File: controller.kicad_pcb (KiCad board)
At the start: 2 copper layers, 59.7 x 49.5 mm, 11 parts, among them J1 Conn_01x03_Male, J2 Conn_01x03_Male, J3 Conn_01x03_Female, J4 Conn_01x03_Male, J5 Conn_01x02_Male

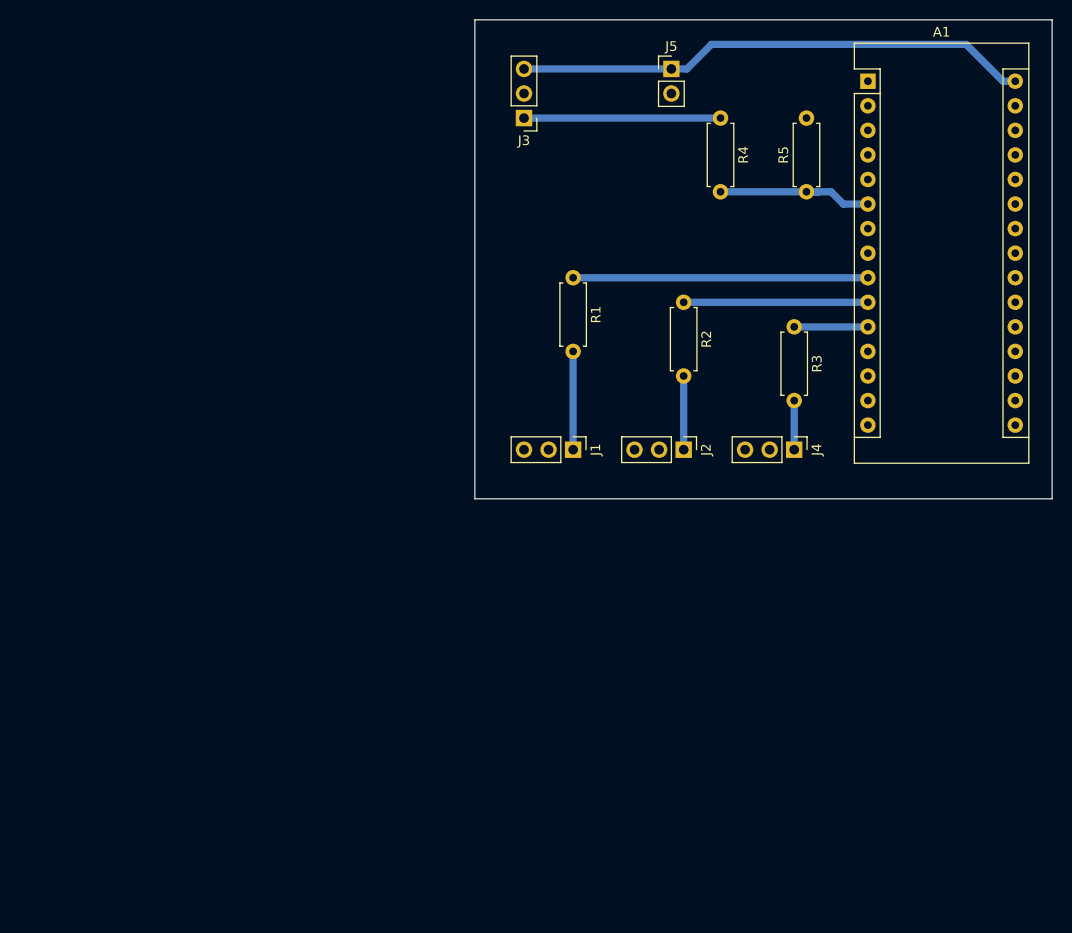
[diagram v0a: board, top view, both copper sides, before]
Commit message: Added max485 and power circuitry
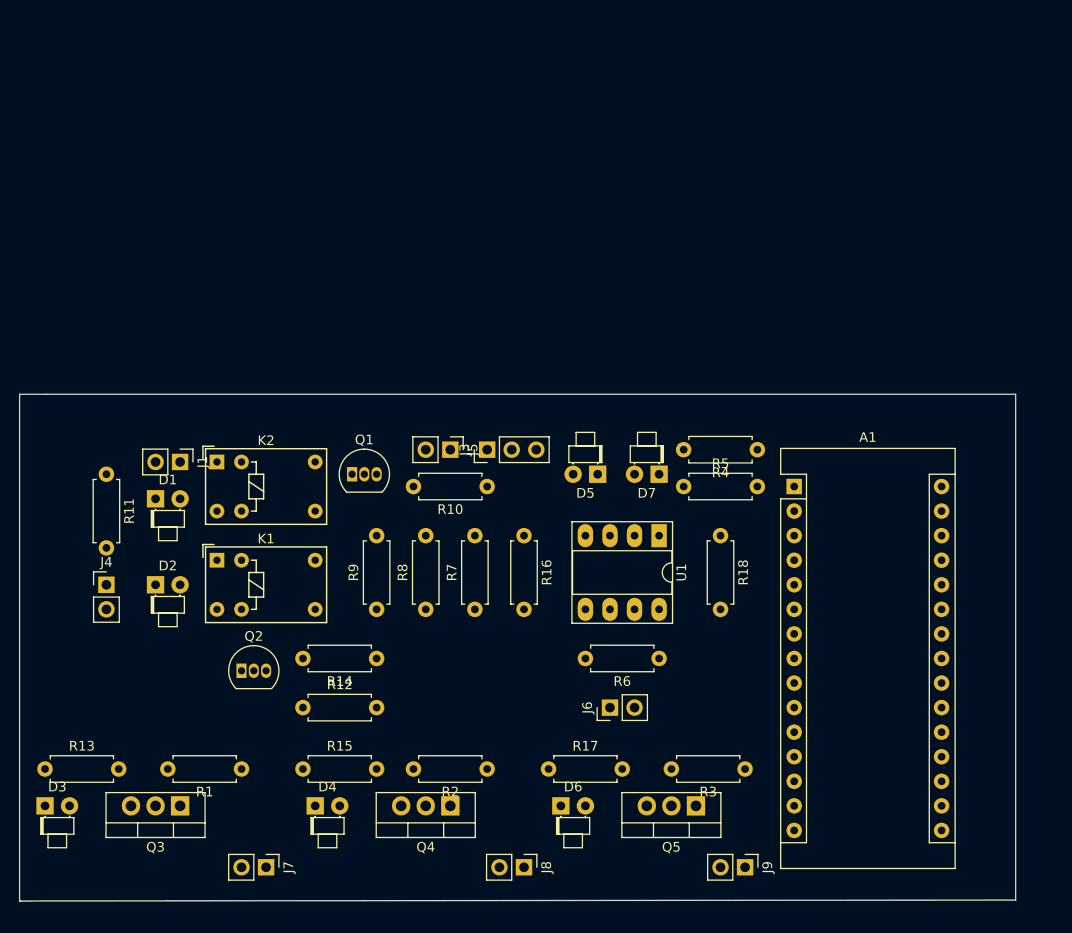
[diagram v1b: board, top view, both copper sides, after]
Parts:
- removed J2: Conn_01x03_Male, Connector_PinHeader_2.54mm:PinHeader_1x03_P2.54mm_Vertical
- added D1: LED, LED_THT:LED_D1.8mm_W1.8mm_H2.4mm_Horizontal_O1.27mm_Z1.6mm, F.Cu at (53.3, 94.0)
- added D2: LED, LED_THT:LED_D1.8mm_W1.8mm_H2.4mm_Horizontal_O1.27mm_Z1.6mm, F.Cu at (53.3, 102.9)
- added D3: LED, LED_THT:LED_D1.8mm_W1.8mm_H2.4mm_Horizontal_O1.27mm_Z1.6mm, F.Cu at (41.9, 125.7)
- added D4: LED, LED_THT:LED_D1.8mm_W1.8mm_H2.4mm_Horizontal_O1.27mm_Z1.6mm, F.Cu at (69.8, 125.7)
- added D5: LED, LED_THT:LED_D1.8mm_W1.8mm_H2.4mm_Horizontal_O1.27mm_Z1.6mm, F.Cu at (99.1, 91.4)
- added D6: LED, LED_THT:LED_D1.8mm_W1.8mm_H2.4mm_Horizontal_O1.27mm_Z1.6mm, F.Cu at (95.2, 125.7)
- added D7: LED, LED_THT:LED_D1.8mm_W1.8mm_H2.4mm_Horizontal_O1.27mm_Z1.6mm, F.Cu at (105.4, 91.4)
- added J6: Conn_01x02, Connector_PinHeader_2.54mm:PinHeader_1x02_P2.54mm_Vertical, F.Cu at (100.3, 115.6)
- added J7: Conn_01x02, Connector_PinHeader_2.54mm:PinHeader_1x02_P2.54mm_Vertical, F.Cu at (64.8, 132.1)
- added J8: Conn_01x02, Connector_PinHeader_2.54mm:PinHeader_1x02_P2.54mm_Vertical, F.Cu at (91.4, 132.1)
- added J9: Conn_01x02, Connector_PinHeader_2.54mm:PinHeader_1x02_P2.54mm_Vertical, F.Cu at (114.3, 132.1)
- added K1: Y14x-1C-xxDS, Relay_THT:Relay_SPDT_HsinDa_Y14, F.Cu at (59.7, 100.3)
- added K2: Y14x-1C-xxDS, Relay_THT:Relay_SPDT_HsinDa_Y14, F.Cu at (59.7, 90.2)
- added Q1: PN2222A, Package_TO_SOT_THT:TO-92_Inline, F.Cu at (73.7, 91.4)
- added Q2: PN2222A, Package_TO_SOT_THT:TO-92_Inline, F.Cu at (62.2, 111.8)
- added Q3: IRF740, Package_TO_SOT_THT:TO-220-3_Vertical, F.Cu at (55.9, 125.7)
- added Q4: IRF740, Package_TO_SOT_THT:TO-220-3_Vertical, F.Cu at (83.8, 125.7)
- added Q5: IRF740, Package_TO_SOT_THT:TO-220-3_Vertical, F.Cu at (109.2, 125.7)
- added R10: 1K, Resistor_THT:R_Axial_DIN0207_L6.3mm_D2.5mm_P7.62mm_Horizontal, F.Cu at (87.6, 92.7)
- added R11: 1K, Resistor_THT:R_Axial_DIN0207_L6.3mm_D2.5mm_P7.62mm_Horizontal, F.Cu at (48.3, 91.4)
- added R12: 1K, Resistor_THT:R_Axial_DIN0207_L6.3mm_D2.5mm_P7.62mm_Horizontal, F.Cu at (68.6, 115.6)
- added R13: 1K, Resistor_THT:R_Axial_DIN0207_L6.3mm_D2.5mm_P7.62mm_Horizontal, F.Cu at (41.9, 121.9)
- added R14: 1K, Resistor_THT:R_Axial_DIN0207_L6.3mm_D2.5mm_P7.62mm_Horizontal, F.Cu at (76.2, 110.5)
- added R15: 1K, Resistor_THT:R_Axial_DIN0207_L6.3mm_D2.5mm_P7.62mm_Horizontal, F.Cu at (68.6, 121.9)
- added R16: 1K, Resistor_THT:R_Axial_DIN0207_L6.3mm_D2.5mm_P7.62mm_Horizontal, F.Cu at (91.4, 97.8)
- added R17: 1K, Resistor_THT:R_Axial_DIN0207_L6.3mm_D2.5mm_P7.62mm_Horizontal, F.Cu at (94.0, 121.9)
- added R18: 1K, Resistor_THT:R_Axial_DIN0207_L6.3mm_D2.5mm_P7.62mm_Horizontal, F.Cu at (111.8, 97.8)
- added R6: R, Resistor_THT:R_Axial_DIN0207_L6.3mm_D2.5mm_P7.62mm_Horizontal, F.Cu at (105.4, 110.5)
- added R7: 10K, Resistor_THT:R_Axial_DIN0207_L6.3mm_D2.5mm_P7.62mm_Horizontal, F.Cu at (86.4, 105.4)
- added R8: 10K, Resistor_THT:R_Axial_DIN0207_L6.3mm_D2.5mm_P7.62mm_Horizontal, F.Cu at (81.3, 105.4)
- added R9: 10K, Resistor_THT:R_Axial_DIN0207_L6.3mm_D2.5mm_P7.62mm_Horizontal, F.Cu at (76.2, 105.4)
- added U1: MAX485E, Package_DIP:DIP-8_W7.62mm_Socket_LongPads, F.Cu at (105.4, 97.8)
- J1, J4: value Conn_01x03_Male -> Conn_01x02; footprint Connector_PinHeader_2.54mm:PinHeader_1x03_P2.54mm_Vertical -> Connector_PinHeader_2.54mm:PinHeader_1x02_P2.54mm_Vertical
- moved J4 72.5 mm to (48.3, 102.9), turned to 0 degrees
- moved R1 61.3 mm to (62.2, 121.9), turned to 180 degrees
- moved R2 52.4 mm to (87.6, 121.9), turned to 180 degrees
- moved R3 46.0 mm to (114.3, 121.9), turned to 180 degrees
- moved J5 45.5 mm to (83.8, 88.9), turned to 270 degrees
- moved A1 42.6 mm to (119.4, 92.7)
- moved J1 40.7 mm to (55.9, 90.2)
- moved J3 34.5 mm to (87.6, 88.9), turned to 90 degrees
- moved R4 34.5 mm to (115.6, 88.9), turned to 180 degrees
- moved R5 33.0 mm to (108.0, 92.7), turned to 0 degrees
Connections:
- J1 pad 1: Net-(J1-Pad1) -> VCC
- J4 pad 1: Net-(J4-Pad1) -> VCC
- R1 pad 1: Net-(A1-Pad9) -> Net-(A1-Pad12)
- R1 pad 2: Net-(J1-Pad1) -> Net-(Q3-Pad1)
- R2 pad 1: Net-(A1-Pad10) -> Net-(A1-Pad13)
- R3 pad 1: Net-(A1-Pad11) -> Net-(A1-Pad14)
- R3 pad 2: Net-(J4-Pad1) -> Net-(Q5-Pad1)
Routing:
- net VCC: track 53.4 -> 0.00 mm
- net Net-(A1-Pad9): track 30.5 -> 0.00 mm
- net Net-(J3-Pad1): track 20.3 -> 0.00 mm
- net Net-(A1-Pad10): track 19.0 -> 0.00 mm
- net Net-(A1-Pad6): track 18.3 -> 0.00 mm
- net Net-(J1-Pad1): track 10.2 -> 0.00 mm
- net Net-(Q4-Pad1): track 7.62 -> 0.00 mm
- net Net-(A1-Pad11): track 7.62 -> 0.00 mm
- net Net-(J4-Pad1): track 5.08 -> 0.00 mm
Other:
- board size 59.7 x 49.5 mm -> 103 x 52.4 mm

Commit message: Added relays symbol and footprint. Re-routed|
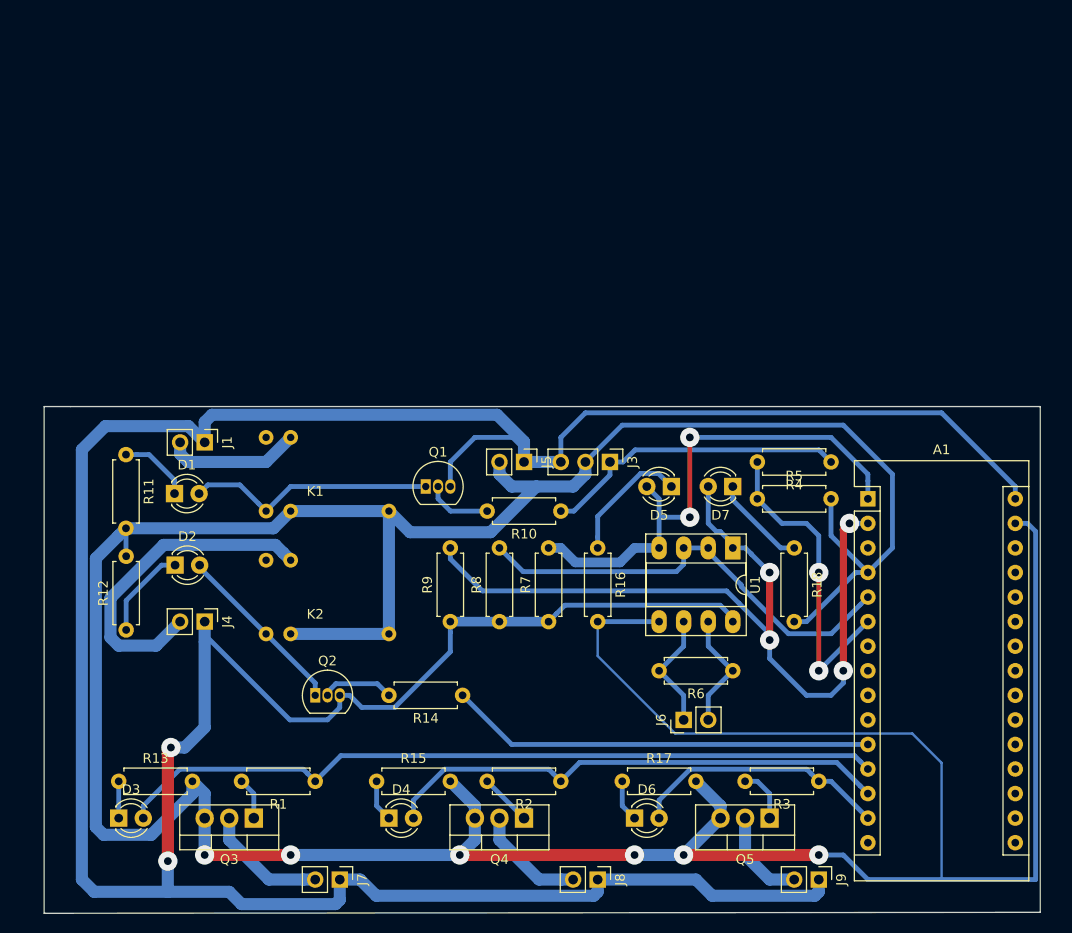
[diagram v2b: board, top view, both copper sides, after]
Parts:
- D1, D2, D3, D4, D5, D6, D7: footprint LED_THT:LED_D1.8mm_W1.8mm_H2.4mm_Horizontal_O1.27mm_Z1.6mm -> LED_THT:LED_D3.0mm
- K1, K2: value Y14x-1C-xxDS -> steren-relay; footprint Relay_THT:Relay_SPDT_HsinDa_Y14 -> controller:steren-relay
- moved R12 20.0 mm to (50.3, 107.5), turned to 90 degrees
- moved K2 18.3 mm to (69.8, 105.4)
- moved J3 12.8 mm to (100.3, 90.2), turned to 270 degrees
- moved K1 12.7 mm to (69.8, 92.7)
- moved J4 10.9 mm to (58.4, 106.7), turned to 270 degrees
- moved R14 9.67 mm to (85.1, 114.3)
- moved R10 8.03 mm to (95.2, 95.2)
- moved Q2 8.03 mm to (69.8, 114.3)
- moved A1 7.73 mm to (127.0, 94.0)
- moved J6 7.73 mm to (108.0, 116.8)
- moved R6 7.73 mm to (113.0, 111.8)
- moved R7 7.73 mm to (94.0, 106.7)
- moved R8 7.73 mm to (88.9, 106.7)
- moved D3 7.73 mm to (49.5, 127.0)
- moved D4 7.73 mm to (77.5, 127.0)
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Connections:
- K1 pad 1: Net-(J4-Pad2) -> Net-(K1-Pad1)
- K1 pad 2: Net-(K1-Pad2) -> Net-(D1-Pad2)
- K1 pad 3: GND -> Net-(J1-Pad2)
- K1 pad 4: Net-(D2-Pad2) -> GND
- K2 pad 1: Net-(J1-Pad2) -> Net-(K2-Pad1)
- K2 pad 2: Net-(K2-Pad2) -> Net-(D2-Pad2)
- K2 pad 3: GND -> Net-(J4-Pad2)
- K2 pad 4: Net-(D1-Pad2) -> GND
- Q2 pad 3: Net-(Q2-Pad3) -> VCC
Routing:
- net GND: track 0.00 -> 410.6 mm, vias 0 -> 6
- net VCC: track 0.00 -> 353.1 mm, vias 0 -> 2
- net Net-(A1-Pad2): track 0.00 -> 88.4 mm, vias 0 -> 4
- net Net-(A1-Pad12): track 0.00 -> 80.0 mm
- net Net-(A1-Pad1): track 0.00 -> 53.5 mm, vias 0 -> 2
- net Net-(A1-Pad13): track 0.00 -> 52.8 mm
- net Net-(A1-Pad5): track 0.00 -> 46.7 mm
- net Net-(A1-Pad11): track 0.00 -> 44.0 mm
- net Net-(J4-Pad2): track 0.00 -> 34.2 mm
- net Net-(A1-Pad6): track 0.00 -> 32.9 mm, vias 0 -> 2
- net Net-(J3-Pad1): track 0.00 -> 31.9 mm
- net Net-(A1-Pad14): track 0.00 -> 26.9 mm
- net Net-(D1-Pad2): track 0.00 -> 26.0 mm
- net Net-(D2-Pad2): track 0.00 -> 18.4 mm
- net Net-(J1-Pad2): track 0.00 -> 14.0 mm
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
